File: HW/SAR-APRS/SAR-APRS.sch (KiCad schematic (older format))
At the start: 14 parts, among them U1 DRA818V, U2 arduino_mini_clone

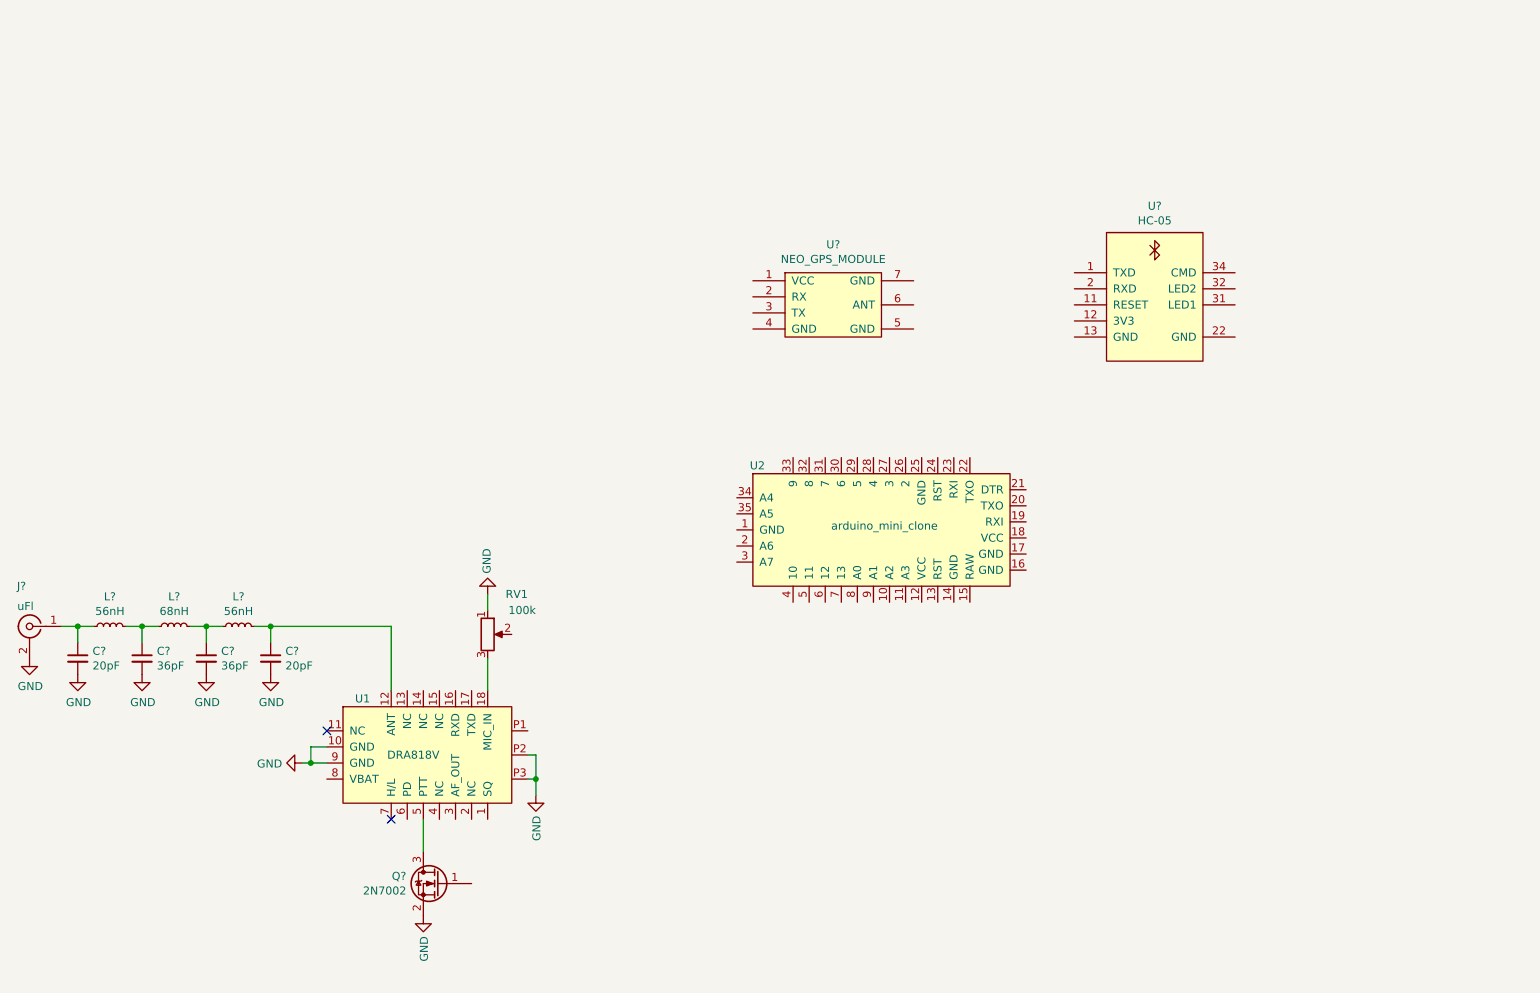
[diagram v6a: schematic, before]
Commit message: schematic update
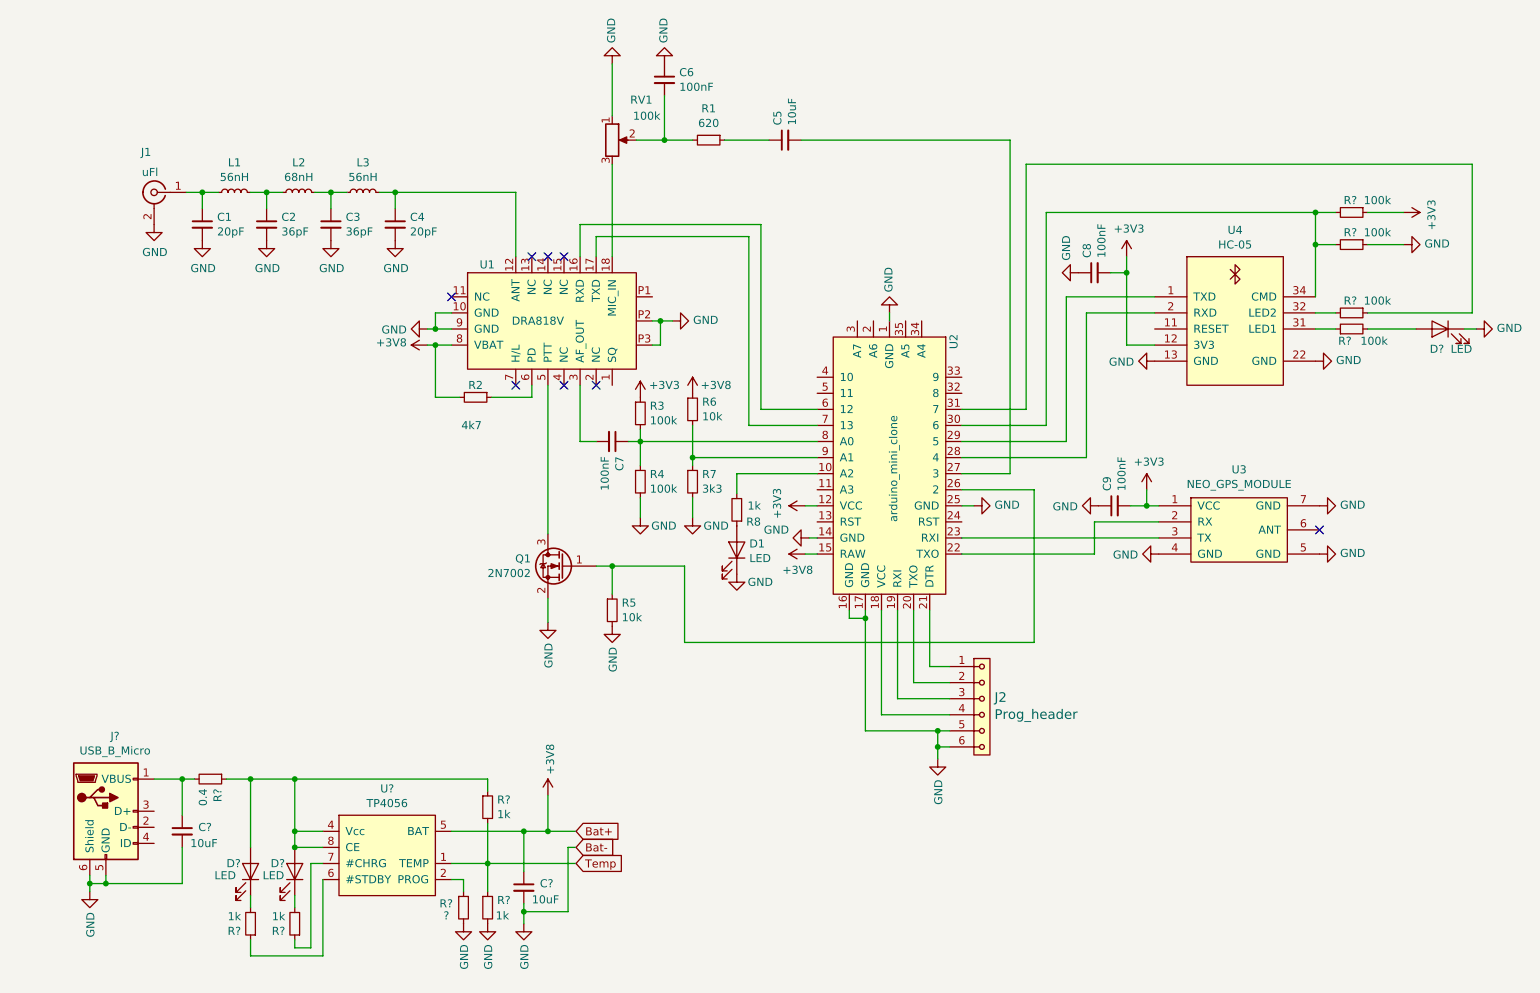
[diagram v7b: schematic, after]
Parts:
- added C5, C? (x2): 10uF, symbol device:C_Small
- added C6, C7, C8, C9: 100nF, symbol device:C_Small
- added D1, D? (x3): LED, symbol device:LED
- added J2: Prog_header, symbol MLAB_HEADER:HEADER_1x06
- added J?: USB_B_Micro, symbol Connector:USB_B_Micro
- added R1: 620, symbol device:R_Small
- added R2: 4k7, symbol device:R_Small
- added R3, R4, R? (x4): 100k, symbol device:R_Small
- added R5, R6: 10k, symbol device:R_Small
- added R7: 3k3, symbol device:R_Small
- added R8, R? (x4): 1k, symbol device:R_Small
- added R?: ?, symbol device:R_Small
- added R?: 0.4, symbol device:R_Small
- added U?: TP4056, symbol APRS_modules:TP4056
- U4: renamed from U?; footprint (none) -> maxrez:HC-05 BT
- gave numbers to parts that had none: 10
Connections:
- net GND: now also U2.1 (GND), U2.14 (GND), U2.16 (GND), U2.17 (GND), U2.25 (GND), U3.4 (GND), U3.5 (GND), U3.7 (GND), U4.13 (GND), U4.22 (GND), C6.1, C8.1, C9.1, C?.2, C?.2, D1.1 (K), D?.1 (K), J2.5, J2.6, J?.5 (GND), J?.6 (Shield), R4.2, R5.2, R7.2, R?.1, R?.2, R?.2
- net at U1.16 (RXD): now also U2.6 (12)
- net at U1.17 (TXD): now also U2.7 (13)
- net at U1.3 (AF_OUT): now also C7.2
- net at U1.6 (PD): now also R2.1
- net +3V8: now reaches U1.8 (VBAT)
- net +3V8: now also U2.15 (RAW), C?.1, R2.2, R6.1, U?.5 (BAT)
- net at U2.10 (A2): now also R8.2
- net +3V3: now reaches U2.12 (VCC)
- net +3V3: now also U3.1 (VCC), U4.12 (3V3), C8.2, C9.2, R3.1, R?.1
- net at U2.18 (VCC): now also J2.4
- net at U2.19 (RXI): now also J2.3
- net at U2.20 (TXO): now also J2.2
- net at U2.21 (DTR): now also J2.1
- net at U2.22 (TXO): now also U3.2 (RX)
- net at U2.23 (RXI): now also U3.3 (TX)
- net at U2.26 (2): now also Q1.1 (G), R5.1
- net at U2.27 (3): now also C5.2
- net at U2.28 (4): now also U4.2 (RXD)
- net at U2.29 (5): now also U4.1 (TXD)
- net at U2.30 (6): now also U4.34 (CMD), R?.2, R?.2
- net at U2.31 (7): now also R?.1
- net at U2.8 (A0): now also C7.1, R3.2, R4.1
- net at U2.9 (A1): now also R6.2, R7.1
- net at RV1.2: now also C6.2, R1.2
- net at U4.31 (LED1): now also R?.1
- net at U4.32 (LED2): now also R?.2
- new net: C5.1, R1.1
- new net: D?.2 (A), R?.2
- new net: R?.1, U?.2 (PROG)
- new net: D1.2 (A), R8.1
- new net: D?.2 (A), D?.2 (A), R?.1, R?.1, U?.4 (Vcc), U?.8 (CE)
- new net: R?.1, U?.6 (#STDBY)
- new net: R?.1, U?.7 (#CHRG)
- new net: C?.1, J?.1 (VBUS), R?.2
- new net: D?.1 (K), R?.2 (x2)
- new net Temp: R?.1, R?.2, U?.1 (TEMP)
- no-connect marks 2 -> 8
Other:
- moved on the sheet: C1, C2, C3, C4, J1, L1, L2, L3, Q1, RV1, U1, U2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

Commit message: schematic update
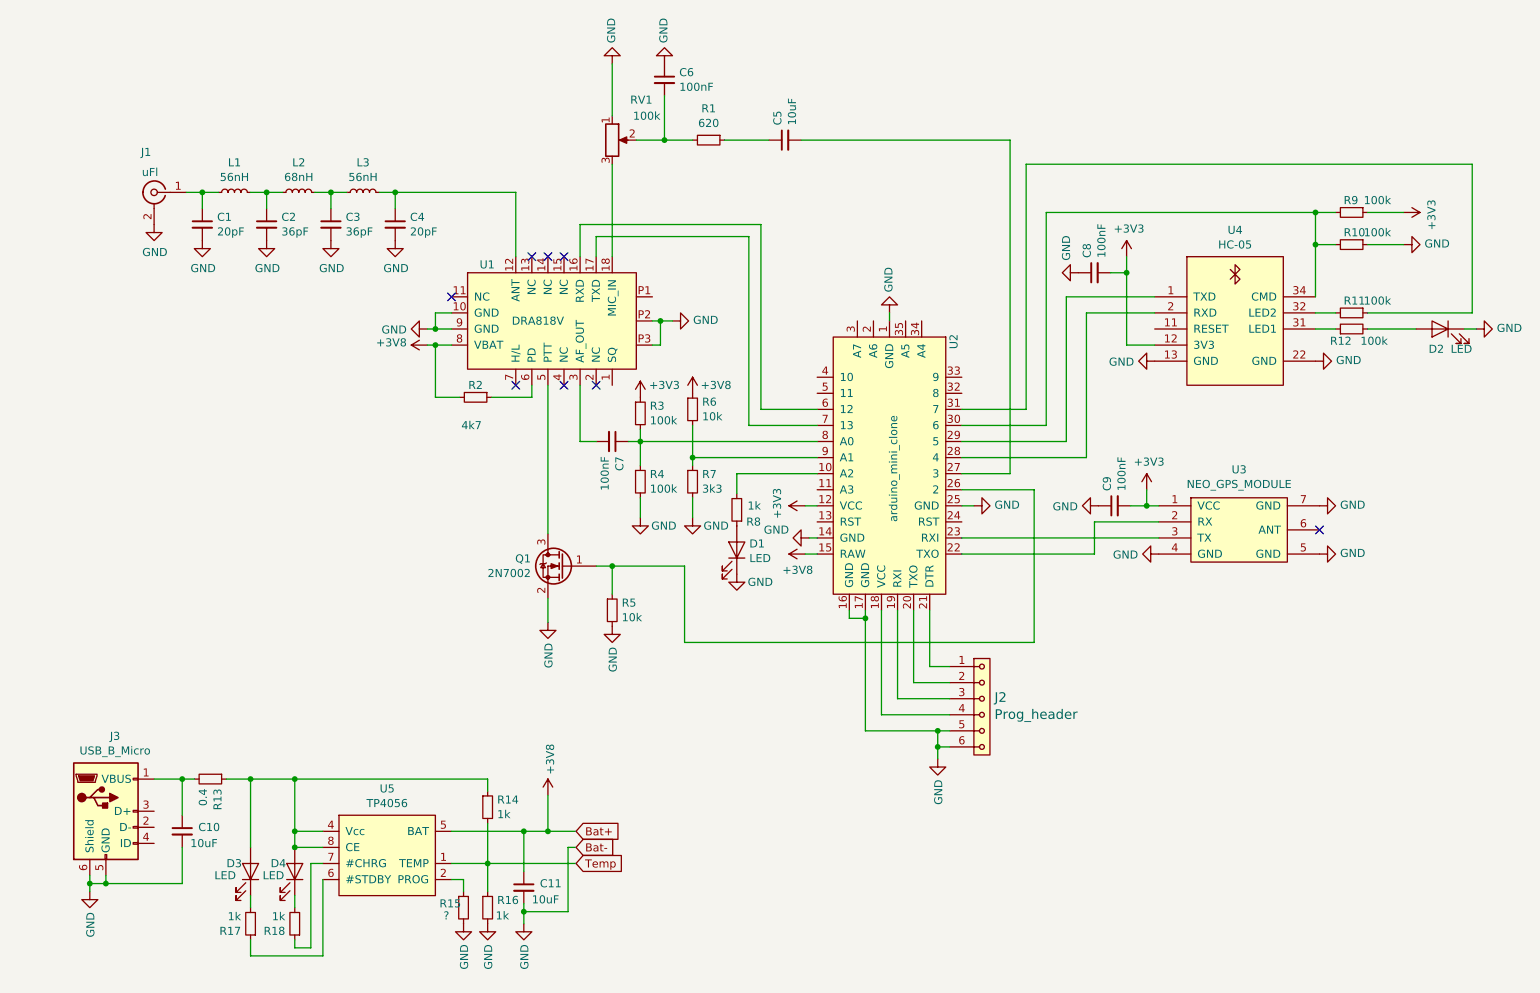
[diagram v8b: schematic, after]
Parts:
- gave numbers to parts that had none: 17
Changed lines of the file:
@@
 	5100 4050 5100 4175
 $Comp
-L device:R_Small R?
+L device:R_Small R11
 U 1 1 5C01ED04
 P 9525 2900
-F 0 "R?" V 9450 2850 50  0000 L CNN
+F 0 "R11" V 9450 2850 50  0000 L CNN
 F 1 "100k" V 9450 2975 50  0000 L CNN
 F 2 "" H 9525 2900 50  0001 C CNN
@@
 $EndComp
 $Comp
-L device:R_Small R?
+L device:R_Small R12
 U 1 1 5C0276B4
 P 9525 3000
-F 0 "R?" V 9450 3000 50  0000 L CNN
+F 0 "R12" V 9450 3000 50  0000 L CNN
 F 1 "100k" V 9450 2775 50  0000 L CNN
 F 2 "" H 9525 3000 50  0001 C CNN
@@
 	9425 3000 9300 3000
 $Comp
-L device:LED D?
+L device:LED D2
 U 1 1 5C03ED62
 P 10075 3000
-F 0 "D?" H 10050 2875 50  0000 L CNN
+F 0 "D2" H 10050 2875 50  0000 L CNN
 F 1 "LED" H 9875 2875 50  0000 L CNN
 F 2 "" H 10075 3000 50  0001 C CNN
@@
 	10300 3000 10225 3000
 $Comp
-L power:GND #PWR?
+L power:GND #PWR0112
 U 1 1 5C04F346
 P 10300 3000
-F 0 "#PWR?" H 10300 2750 50  0001 C CNN
+F 0 "#PWR0112" H 10300 2750 50  0001 C CNN
 F 1 "GND" V 10305 2872 50  0000 R CNN
 F 2 "" H 10300 3000 50  0001 C CNN
@@
 	7625 3600 7625 2275
 $Comp
-L device:R_Small R?
+L device:R_Small R10
 U 1 1 5C066ABE
 P 9525 2475
-F 0 "R?" V 9450 2425 50  0000 L CNN
+F 0 "R10" V 9450 2425 50  0000 L CNN
 F 1 "100k" V 9450 2550 50  0000 L CNN
 F 2 "" H 9525 2475 50  0001 C CNN
@@
 $EndComp
 $Comp
-L device:R_Small R?
+L device:R_Small R9
 U 1 1 5C06896B
 P 9525 2275
-F 0 "R?" V 9450 2225 50  0000 L CNN
+F 0 "R9" V 9450 2225 50  0000 L CNN
 F 1 "100k" V 9450 2350 50  0000 L CNN
 F 2 "" H 9525 2275 50  0001 C CNN
@@
 $EndComp
 $Comp
-L power:GND #PWR?
+L power:GND #PWR0134
 U 1 1 5C0721C1
 P 9850 2475
-F 0 "#PWR?" H 9850 2225 50  0001 C CNN
+F 0 "#PWR0134" H 9850 2225 50  0001 C CNN
 F 1 "GND" V 9855 2347 50  0000 R CNN
 F 2 "" H 9850 2475 50  0001 C CNN
@@
 	9850 2475 9625 2475
 $Comp
-L power:+3V3 #PWR?
+L power:+3V3 #PWR0135
 U 1 1 5C078D1B
 P 9850 2275
-F 0 "#PWR?" H 9850 2125 50  0001 C CNN
+F 0 "#PWR0135" H 9850 2125 50  0001 C CNN
 F 1 "+3V3" H 9865 2448 50  0000 C CNN
 F 2 "" H 9850 2275 50  0001 C CNN
@@
 	9625 2900 10275 2900
 $Comp
-L APRS_modules:TP4056 U?
+L APRS_modules:TP4056 U5
 U 1 1 5C0CA488
 P 3525 6275
-F 0 "U?" H 3525 6690 50  0000 C CNN
+F 0 "U5" H 3525 6690 50  0000 C CNN
 F 1 "TP4056" H 3525 6599 50  0000 C CNN
 F 2 "" H 2975 6675 50  0001 C CNN
@@
 	2950 6125 3125 6125
 $Comp
-L device:R_Small R?
+L device:R_Small R15
 U 1 1 5C0989BF
 P 4000 6600
-F 0 "R?" H 3850 6625 50  0000 L CNN
+F 0 "R15" H 3850 6625 50  0000 L CNN
 F 1 "?" H 3875 6550 50  0000 L CNN
 F 2 "" H 4000 6600 50  0001 C CNN
@@
 $EndComp
 $Comp
-L device:R_Small R?
+L device:R_Small R16
 U 1 1 5C09DA48
 P 4150 6600
-F 0 "R?" H 4209 6646 50  0000 L CNN
+F 0 "R16" H 4209 6646 50  0000 L CNN
 F 1 "1k" H 4200 6550 50  0000 L CNN
 F 2 "" H 4150 6600 50  0001 C CNN
@@
 	4000 6425 4000 6500
 $Comp
-L power:GND #PWR?
+L power:GND #PWR0136
 U 1 1 5C0A2F76
 P 4000 6700
-F 0 "#PWR?" H 4000 6450 50  0001 C CNN
+F 0 "#PWR0136" H 4000 6450 50  0001 C CNN
 F 1 "GND" V 4005 6572 50  0000 R CNN
 F 2 "" H 4000 6700 50  0001 C CNN
@@
 $EndComp
 $Comp
-L power:GND #PWR?
+L power:GND #PWR0137
 U 1 1 5C0A5A2D
 P 4150 6700
-F 0 "#PWR?" H 4150 6450 50  0001 C CNN
+F 0 "#PWR0137" H 4150 6450 50  0001 C CNN
 F 1 "GND" V 4155 6572 50  0000 R CNN
 F 2 "" H 4150 6700 50  0001 C CNN
@@
 $EndComp
 $Comp
-L device:R_Small R?
+L device:R_Small R14
 U 1 1 5C0A6498
 P 4150 5975
-F 0 "R?" H 4209 6021 50  0000 L CNN
+F 0 "R14" H 4209 6021 50  0000 L CNN
 F 1 "1k" H 4209 5930 50  0000 L CNN
 F 2 "" H 4150 5975 50  0001 C CNN
@@
 	4150 6325 4150 6500
 $Comp
-L device:C_Small C?
+L device:C_Small C11
 U 1 1 5C0C92DE
 P 4375 6475
-F 0 "C?" H 4475 6500 50  0000 L CNN
+F 0 "C11" H 4475 6500 50  0000 L CNN
 F 1 "10uF" H 4425 6400 50  0000 L CNN
 F 2 "" H 4375 6475 50  0001 C CNN
@@
 $EndComp
 $Comp
-L power:GND #PWR?
+L power:GND #PWR0138
 U 1 1 5C0D4401
 P 4375 6700
-F 0 "#PWR?" H 4375 6450 50  0001 C CNN
+F 0 "#PWR0138" H 4375 6450 50  0001 C CNN
 F 1 "GND" V 4380 6572 50  0000 R CNN
 F 2 "" H 4375 6700 50  0001 C CNN
@@
 Connection ~ 2950 6125
 $Comp
-L device:R_Small R?
+L device:R_Small R13
 U 1 1 5C0EF0DF
 P 2425 5800
-F 0 "R?" H 2484 5846 50  0000 L CNN
+F 0 "R13" H 2484 5846 50  0000 L CNN
 F 1 "0.4" H 2484 5755 50  0000 L CNN
 F 2 "" H 2425 5800 50  0001 C CNN
@@
 	4375 6625 4375 6700
 $Comp
-L power:+3V8 #PWR?
+L power:+3V8 #PWR0139
 U 1 1 5C1369FF
 P 4525 5900
-F 0 "#PWR?" H 4525 5750 50  0001 C CNN
+F 0 "#PWR0139" H 4525 5750 50  0001 C CNN
 F 1 "+3V8" V 4540 6028 50  0000 L CNN
 F 2 "" H 4525 5900 50  0001 C CNN
@@
 	4525 6125 4700 6125
 $Comp
-L Connector:USB_B_Micro J?
+L Connector:USB_B_Micro J3
 U 1 1 5C14B180
 P 1775 6000
-F 0 "J?" H 1832 6467 50  0000 C CNN
+F 0 "J3" H 1832 6467 50  0000 C CNN
 F 1 "USB_B_Micro" H 1832 6376 50  0000 C CNN
 F 2 "" H 1925 5950 50  0001 C CNN
@@
 	2325 5800 2250 5800
 $Comp
-L power:GND #PWR?
+L power:GND #PWR0140
 U 1 1 5C168AAF
 P 1675 6500
-F 0 "#PWR?" H 1675 6250 50  0001 C CNN
+F 0 "#PWR0140" H 1675 6250 50  0001 C CNN
 F 1 "GND" V 1680 6372 50  0000 R CNN
 F 2 "" H 1675 6500 50  0001 C CNN
@@
 	1675 6450 1675 6500
 $Comp
-L device:C_Small C?
+L device:C_Small C10
 U 1 1 5C1764A3
 P 2250 6125
-F 0 "C?" H 2350 6150 50  0000 L CNN
+F 0 "C10" H 2350 6150 50  0000 L CNN
 F 1 "10uF" H 2300 6050 50  0000 L CNN
 F 2 "" H 2250 6125 50  0001 C CNN
@@
 Connection ~ 1775 6450
 $Comp
-L device:LED D?
+L device:LED D4
 U 1 1 5C1981BB
 P 2950 6375
-F 0 "D?" V 3000 6225 50  0000 L CNN
+F 0 "D4" V 3000 6225 50  0000 L CNN
 F 1 "LED" V 2925 6175 50  0000 L CNN
 F 2 "" H 2950 6375 50  0001 C CNN
@@
 $EndComp
 $Comp
-L device:LED D?
+L device:LED D3
 U 1 1 5C19FD9F
 P 2675 6375
-F 0 "D?" V 2725 6225 50  0000 L CNN
+F 0 "D3" V 2725 6225 50  0000 L CNN
 F 1 "LED" V 2650 6150 50  0000 L CNN
 F 2 "" H 2675 6375 50  0001 C CNN
@@
 Connection ~ 2950 6225
 $Comp
-L device:R_Small R?
+L device:R_Small R18
 U 1 1 5C1BBD5A
 P 2950 6700
-F 0 "R?" H 3009 6746 50  0000 L CNN
+F 0 "R18" H 3009 6746 50  0000 L CNN
 F 1 "1k" H 3009 6655 50  0000 L CNN
 F 2 "" H 2950 6700 50  0001 C CNN
@@
 	3050 6325 3125 6325
 $Comp
-L device:R_Small R?
+L device:R_Small R17
 U 1 1 5C1DE600
 P 2675 6700
-F 0 "R?" H 2734 6746 50  0000 L CNN
+F 0 "R17" H 2734 6746 50  0000 L CNN
 F 1 "1k" H 2734 6655 50  0000 L CNN
 F 2 "" H 2675 6700 50  0001 C CNN
